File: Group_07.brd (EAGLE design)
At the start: 76.2 x 77.5 mm, 29 parts, among them J1 POWER_JACKPTH_LOCK, U1 +12v, U3 TCA9546ASO16, U4 TMUX1208

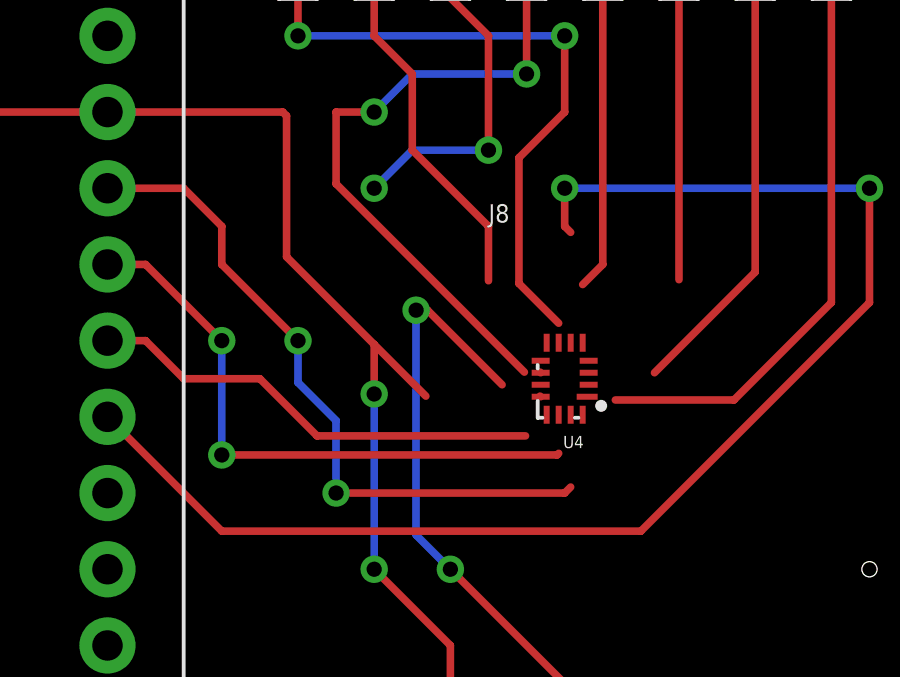
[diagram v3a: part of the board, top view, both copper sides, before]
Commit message: airwire fixed by replacing w/ width 8 instead of 10
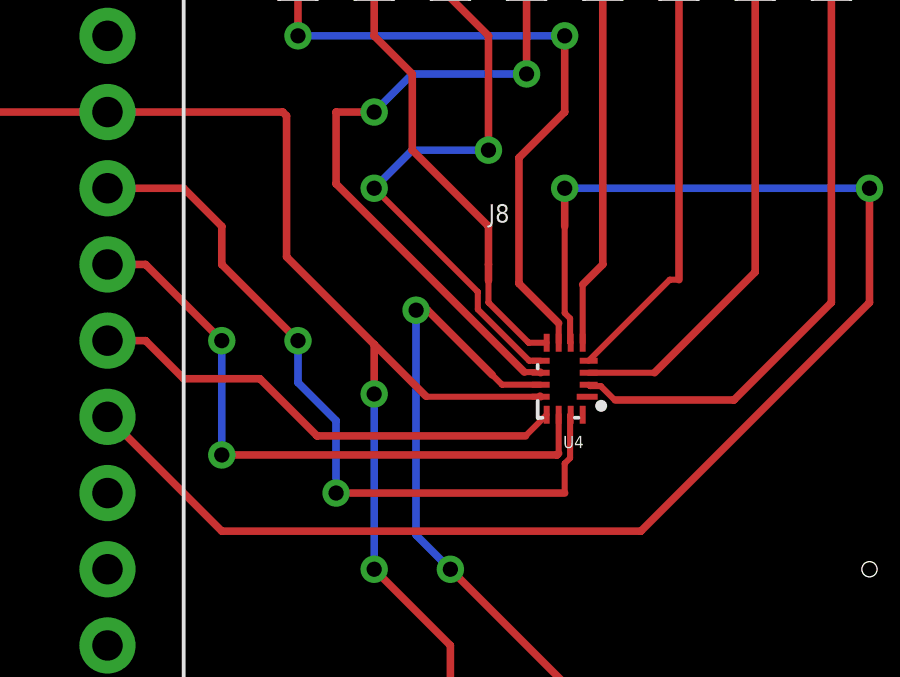
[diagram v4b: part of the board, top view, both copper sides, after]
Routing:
- net N$15: track 11.5 -> 19.6 mm
- net N$12: track 10.5 -> 14.7 mm
- net GND: track 212.9 -> 216.8 mm
- net N$16: track 12.2 -> 15.9 mm
- net MUX_OUT/1.4C: track 45.7 -> 49.3 mm
- net MUX_A0/1.3C: track 22.7 -> 25.1 mm
- net N$11: track 15.3 -> 17.5 mm
- net N$13: track 11.2 -> 13.2 mm
- net MUX_A1/1.4C: track 19.9 -> 21.2 mm
- net 5V: track 297.2 -> 298.5 mm
- net N$2: track 19.8 -> 20.9 mm
- net MUX_A2/1.4C: track 15.3 -> 16.2 mm
- net N$17: track 22.3 -> 23.0 mm
- net N$14: track 21.9 -> 22.4 mm

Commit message: all fixed w/ width8
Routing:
- net N$16: track 15.9 -> 15.4 mm
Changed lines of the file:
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@@
 <wire x1="66.04" y1="49.53" x2="66.04" y2="45.72" width="0.254" layer="1"/>
 <wire x1="66.04" y1="45.72" x2="66.04" y2="44.03" width="0.254" layer="1"/>
-<wire x1="57.658" y1="61.976" x2="59.817" y2="59.817" width="0.254" layer="1"/>
+<wire x1="59.817" y1="59.817" x2="57.658" y2="61.976" width="0.254" layer="1"/>
 <wire x1="6.858" y1="44.45" x2="6.858" y2="41.656" width="0.254" layer="1"/>
 <via x="6.858" y="41.656" extent="1-16" drill="0.508"/>
@@
 <wire x1="7.62" y1="31.75" x2="7.62" y2="15.24" width="0.254" layer="16"/>
 <wire x1="8.509" y1="11.811" x2="10.789" y2="11.811" width="0.254" layer="1"/>
-<wire x1="59.817" y1="59.817" x2="60.1424" y2="59.4916" width="0.2032" layer="1"/>
-<wire x1="60.1424" y1="59.4916" x2="61.43" y2="59.4916" width="0.2032" layer="1"/>
-<wire x1="61.43" y1="59.4916" x2="61.43" y2="59.49" width="0" layer="19" extent="1-1"/>
+<wire x1="61.43" y1="59.49" x2="60.144" y2="59.49" width="0.2032" layer="1"/>
+<wire x1="60.144" y1="59.49" x2="59.817" y2="59.817" width="0.2032" layer="1"/>
 </signal>
 <signal name="N$1">
@@
 <vertex x="76.2" y="0"/>
 </polygon>
-<wire x1="61.43" y1="59.09" x2="61.4094" y2="59.1106" width="0.254" layer="1"/>
 <wire x1="55.88" y1="60.833" x2="57.6024" y2="59.1106" width="0.254" layer="1"/>
 <wire x1="55.88" y1="60.833" x2="52.959" y2="63.754" width="0.254" layer="1"/>
@@
 <contactref element="J8" pad="4"/>
 <contactref element="U4" pad="10"/>
-<wire x1="61.4094" y1="59.9106" x2="61.43" y2="59.89" width="0.254" layer="1"/>
-<wire x1="54.61" y1="66.18786875" x2="60.88726875" y2="59.9106" width="0.254" layer="1"/>
-<wire x1="54.61" y1="66.18786875" x2="54.61" y2="68.58" width="0.254" layer="1"/>
-<wire x1="54.61" y1="68.58" x2="55.88" y2="68.58" width="0.254" layer="1"/>
+<wire x1="55.88" y1="68.58" x2="54.61" y2="68.58" width="0.254" layer="1"/>
 <via x="55.88" y="68.58" extent="1-16" drill="0.508"/>
 <wire x1="55.88" y1="68.58" x2="57.15" y2="69.85" width="0.254" layer="16"/>
@@
 <wire x1="60.96" y1="69.85" x2="60.96" y2="73.533" width="0.254" layer="1"/>
 <wire x1="57.15" y1="69.85" x2="60.96" y2="69.85" width="0.254" layer="16"/>
-<wire x1="60.88726875" y1="59.9106" x2="61.4094" y2="59.9106" width="0.2032" layer="1"/>
+<wire x1="60.76" y1="59.89" x2="61.43" y2="59.89" width="0.254" layer="1"/>
+<wire x1="54.61" y1="68.58" x2="54.61" y2="66.04" width="0.254" layer="1"/>
+<wire x1="54.61" y1="66.04" x2="60.76" y2="59.89" width="0.254" layer="1"/>
 </signal>
 <signal name="N$15">
@@
 <wire x1="59.69" y1="67.31" x2="59.69" y2="71.12" width="0.254" layer="1"/>
 <wire x1="55.88" y1="66.04" x2="59.3344" y2="62.5856" width="0.2032" layer="1"/>
-<wire x1="59.3344" y1="62.5856" x2="59.3344" y2="62.0022875" width="0.2032" layer="1"/>
-<wire x1="61.0450875" y1="60.2916" x2="61.43" y2="60.2916" width="0.2032" layer="1"/>
-<wire x1="59.3344" y1="62.0022875" x2="61.0450875" y2="60.2916" width="0.2032" layer="1"/>
-<wire x1="61.43" y1="60.2916" x2="61.43" y2="60.29" width="0" layer="19" extent="1-1"/>
+<wire x1="59.3344" y1="62.0022875" x2="59.3344" y2="62.5856" width="0.2032" layer="1"/>
+<wire x1="61.43" y1="60.29" x2="61.0466875" y2="60.29" width="0.2032" layer="1"/>
+<wire x1="61.0466875" y1="60.29" x2="59.3344" y2="62.0022875" width="0.2032" layer="1"/>
 </signal>
 <signal name="N$16">
 <contactref element="J8" pad="2"/>
 <contactref element="U4" pad="8"/>
-<wire x1="59.69" y1="64.77" x2="59.69" y2="63.5" width="0.254" layer="1"/>
-<wire x1="59.69" y1="62.957" x2="59.69" y2="63.5" width="0.254" layer="1"/>
 <wire x1="57.15" y1="69.85" x2="55.88" y2="71.12" width="0.254" layer="1"/>
 <wire x1="55.88" y1="71.12" x2="55.88" y2="73.533" width="0.254" layer="1"/>
-<wire x1="59.69" y1="64.77" x2="57.15" y2="67.31" width="0.254" layer="1"/>
+<wire x1="57.15" y1="67.31" x2="59.69" y2="64.77" width="0.254" layer="1"/>
 <wire x1="57.15" y1="67.31" x2="57.15" y2="69.85" width="0.254" layer="1"/>
-<wire x1="59.69" y1="63.5" x2="59.69" y2="62.23" width="0.2032" layer="1"/>
 <wire x1="59.69" y1="62.23" x2="61.03" y2="60.89" width="0.2032" layer="1"/>
 <wire x1="61.03" y1="60.89" x2="61.63" y2="60.89" width="0.2032" layer="1"/>
+<wire x1="59.69" y1="64.77" x2="59.69" y2="62.23" width="0.2032" layer="1"/>
 </signal>
 <signal name="N$17">

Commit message: Disposizione modificata
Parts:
- moved J7 60.2 mm to (59.8, 29.5), turned to 90 degrees
- moved C1 60.1 mm to (59.7, 67.9)
- moved U1 43.0 mm to (4.95, 50.5), turned to 180 degrees
- moved C3 39.1 mm to (3.81, 14.2)
- moved J4 37.4 mm to (59.7, 3.81)
- moved R4 37.0 mm to (55.9, 7.62)
- moved R5 35.8 mm to (55.9, 3.81), turned to 90 degrees
- moved J3 24.4 mm to (59.7, 10.2), turned to 90 degrees
- moved R3 23.7 mm to (55.9, 11.6), turned to 90 degrees
- moved U3 21.2 mm to (48.4, 19.4), turned to 90 degrees
- moved J6 19.8 mm to (59.9, 25.4), turned to 270 degrees
- moved C2 19.6 mm to (11.8, 55.1)
- moved R10 19.5 mm to (10.8, 48.8), turned to 270 degrees
- moved R2 16.3 mm to (55.9, 15.2)
- moved S1 14.6 mm to (3.94, 64.0)
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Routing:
- net 5V: track 298.5 -> 0.00 mm, vias 18 -> 0
- net GND: track 216.7 -> 0.00 mm, vias 11 -> 0
- net I2C_SDA_3: track 51.0 -> 0.00 mm, vias 2 -> 0
- net 12V: track 50.2 -> 0.00 mm, vias 4 -> 0
- net I2C_SDA_2: track 50.2 -> 0.00 mm, vias 2 -> 0
- net MUX_OUT/1.4C: track 49.3 -> 0.00 mm, vias 2 -> 0
- net PHOTO_OUT: track 43.9 -> 0.00 mm, vias 2 -> 0
- net I2C_SCL_2: track 38.6 -> 0.00 mm, vias 2 -> 0
- net I2C_SCL_3: track 36.8 -> 0.00 mm, vias 2 -> 0
- net I2C_A2: track 31.1 -> 0.00 mm, vias 2 -> 0
- net MUX_A0/1.3C: track 25.1 -> 0.00 mm, vias 2 -> 0
- net N$8: track 23.6 -> 0.00 mm
- net N$4: track 23.6 -> 0.00 mm
- net N$6: track 23.6 -> 0.00 mm
- net N$5: track 23.3 -> 0.00 mm
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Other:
- board size 76.2 x 77.5 mm -> 63.5 x 74.9 mm

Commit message: Connessioni TCA9546A
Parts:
- moved R3 7.73 mm to (54.6, 3.94)
- moved R2 7.73 mm to (54.6, 7.62)
- moved R4 7.73 mm to (54.6, 15.2)
- moved R5 7.73 mm to (54.6, 11.4)
- moved J3 6.48 mm to (58.4, 3.81)
- moved J4 6.48 mm to (58.4, 10.2)
- moved C3 5.08 mm to (3.81, 9.14)
- moved J2 5.08 mm to (3.81, 14.4)
- moved R6 4.02 mm to (54.6, 22.9)
- moved R7 4.02 mm to (54.6, 19.1)
- moved R8 4.02 mm to (54.6, 30.5)
- moved R9 4.02 mm to (54.6, 26.7)
- moved J6 2.84 mm to (58.7, 22.9), turned to 90 degrees
- moved J5 2.84 mm to (58.4, 16.5), turned to 90 degrees
- moved C1 1.80 mm to (58.4, 66.7)
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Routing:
- net 5V: track 0.00 -> 63.0 mm, vias 0 -> 10
- net I2C_SCL: track 0.00 -> 23.3 mm
- net I2C_SDA_0: track 0.00 -> 22.5 mm
- net I2C_SDA: track 0.00 -> 20.1 mm
- net I2C_SCL_3: track 0.00 -> 18.3 mm
- net I2C_SCL_0: track 0.00 -> 18.0 mm
- net I2C_SDA_2: track 0.00 -> 16.1 mm
- net I2C_SCL_2: track 0.00 -> 15.4 mm
- net I2C_SDA_3: track 0.00 -> 13.9 mm
- net I2C_SDA_1: track 0.00 -> 13.5 mm
- net I2C_A1: track 0.00 -> 13.1 mm, vias 0 -> 2
- net I2C_A2: track 0.00 -> 12.9 mm, vias 0 -> 2
- net I2C_SCL_1: track 0.00 -> 11.0 mm
- net I2C_A0: track 0.00 -> 5.42 mm
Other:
- board size 63.5 x 74.9 mm -> 62.2 x 74.9 mm

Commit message: modifiche tmux
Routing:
- net GND: track 0.00 -> 27.1 mm
- net N$2: track 0.00 -> 24.4 mm
- net MUX_OUT/1.4C: track 0.00 -> 22.2 mm, vias 0 -> 2
- net N$11: track 0.00 -> 22.1 mm
- net N$14: track 0.00 -> 20.7 mm, vias 0 -> 2
- net N$12: track 0.00 -> 19.8 mm
- net N$15: track 0.00 -> 17.8 mm, vias 0 -> 2
- net N$13: track 0.00 -> 17.2 mm
- net 5V: track 63.0 -> 77.6 mm
- net N$17: track 0.00 -> 12.8 mm, vias 0 -> 2
- net N$16: track 0.00 -> 12.1 mm
- net MUX_A0/1.3C: track 0.00 -> 10.5 mm, vias 0 -> 2
- net MUX_A2/1.4C: track 0.00 -> 9.07 mm, vias 0 -> 2
- net MUX_A1/1.4C: track 0.00 -> 5.91 mm
